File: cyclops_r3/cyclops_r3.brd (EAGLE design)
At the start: 124.5 x 79.9 mm, 107 parts, among them Q1 BC817, Q2 IRF510, U1 MCP4921, U2 MCP4022-50k, U3 317-N, U4 TLV3701, U5 337-N, U6 ADR03, U7 OP1177, U8 LTC2052HV, U9 ZXTD45

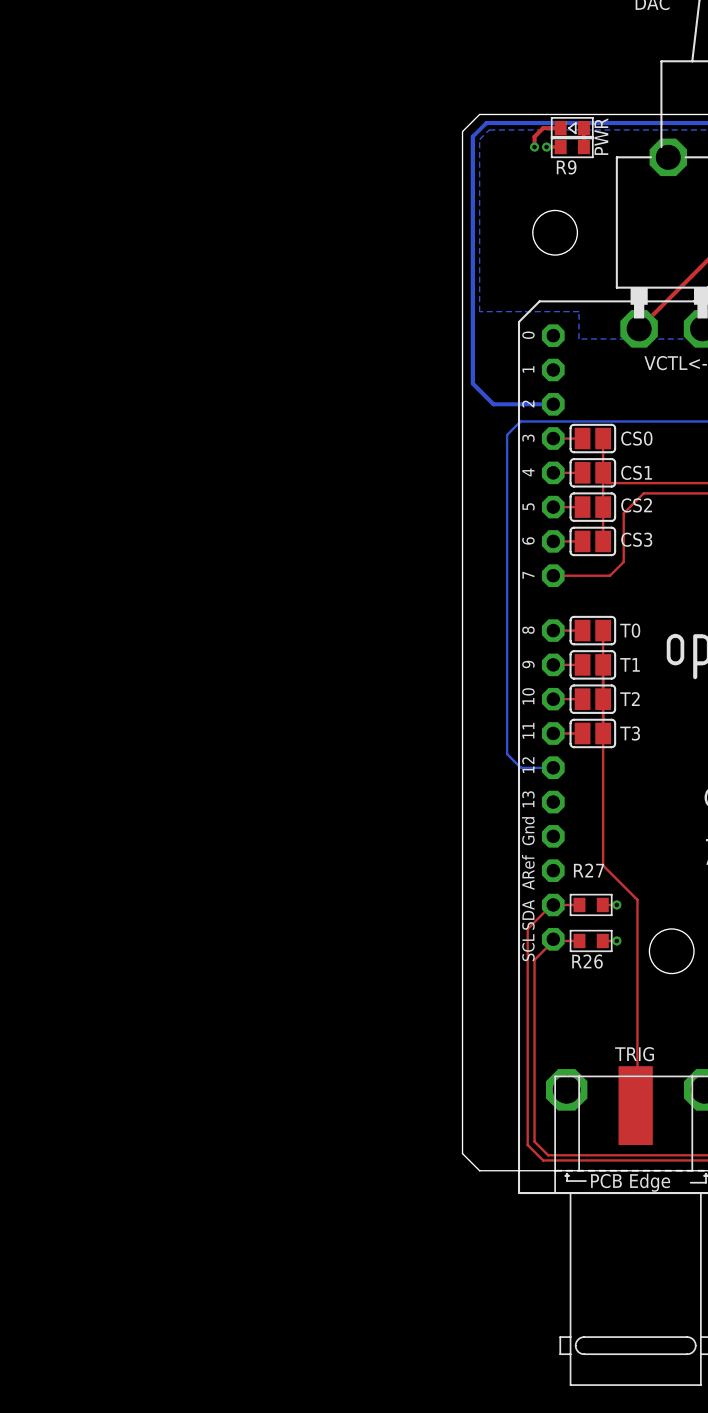
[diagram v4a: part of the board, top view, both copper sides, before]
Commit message: Front panel dimensions have been tested and look good. Started integrating light pipes on front panel LEDs. The LEDs need to be moved and swapped for normal verical ones.
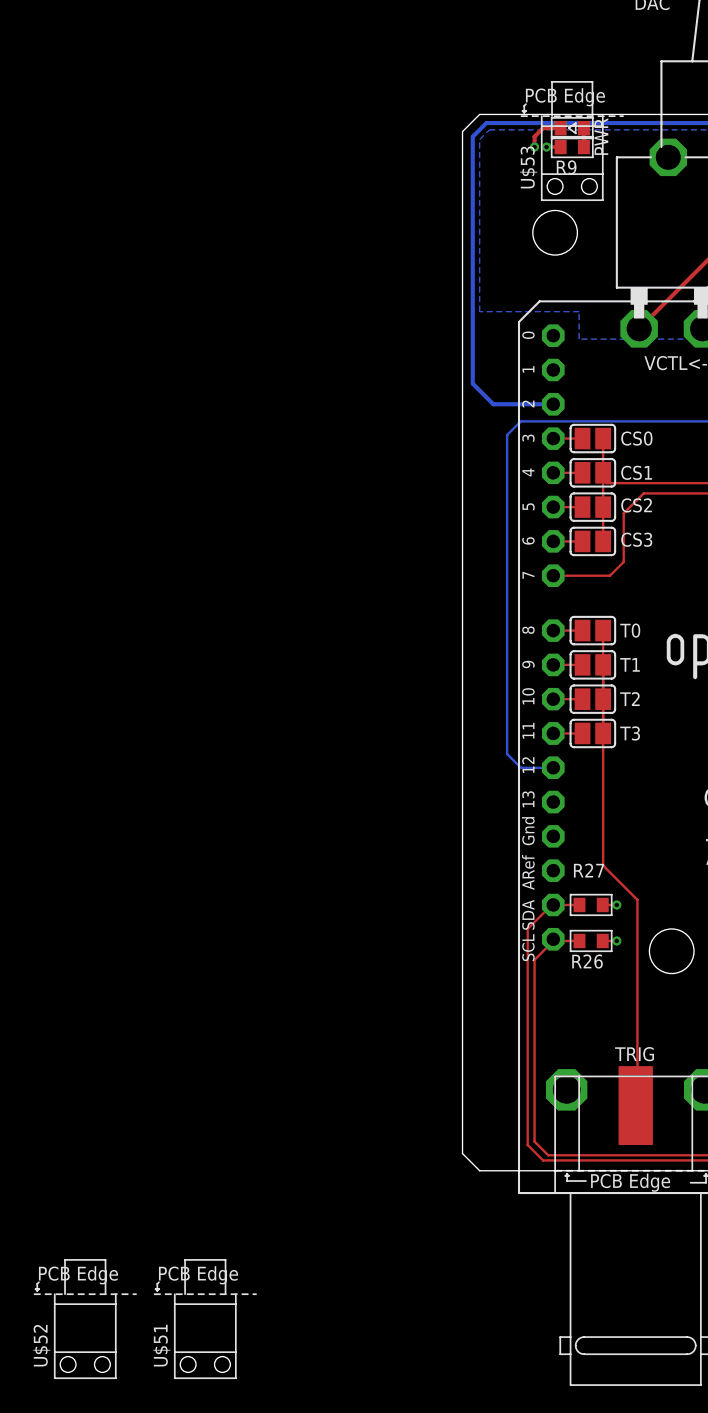
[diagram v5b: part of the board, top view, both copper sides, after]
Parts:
- added U$51, U$52, U$53: SLP3, cyclops:SL3P-150-100-F
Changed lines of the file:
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@@
 <?xml version="1.0" encoding="utf-8"?>
 <!DOCTYPE eagle SYSTEM "eagle.dtd">
-<eagle version="6.6.0">
+<eagle version="6.5.0">
 <drawing>
 <settings>
@@
 <setting verticaltext="up"/>
 </settings>
-<grid distance="0.05" unitdist="inch" unit="inch" style="lines" multiple="1" display="yes" altdistance="0.025" altunitdist="inch" altunit="inch"/>
+<grid distance="0.005" unitdist="inch" unit="inch" style="lines" multiple="1" display="yes" altdistance="0.025" altunitdist="inch" altunit="inch"/>
 <layers>
 <layer number="1" name="Top" color="4" fill="1" visible="yes" active="yes"/>
@@
 <layer number="37" name="tTest" color="7" fill="1" visible="no" active="yes"/>
 <layer number="38" name="bTest" color="7" fill="1" visible="no" active="yes"/>
-<layer number="39" name="tKeepout" color="4" fill="11" visible="no" active="yes"/>
+<layer number="39" name="tKeepout" color="4" fill="11" visible="yes" active="yes"/>
 <layer number="40" name="bKeepout" color="1" fill="11" visible="no" active="yes"/>
 <layer number="41" name="tRestrict" color="4" fill="10" visible="no" active="yes"/>
@@
 <attribute name="VALUE" x="8.128" y="22.733" size="1.016" layer="27" font="vector" ratio="18" align="center-left"/>
 </element>
+<element name="U$51" library="cyclops" package="SL3P-150-100-F" value="SLP3" x="-19.05" y="-12.7"/>
+<element name="U$52" library="cyclops" package="SL3P-150-100-F" value="SLP3" x="-27.94" y="-12.7"/>
+<element name="U$53" library="cyclops" package="SL3P-150-100-F" value="SLP3" x="8.128" y="74.549"/>
 </elements>
 <signals>

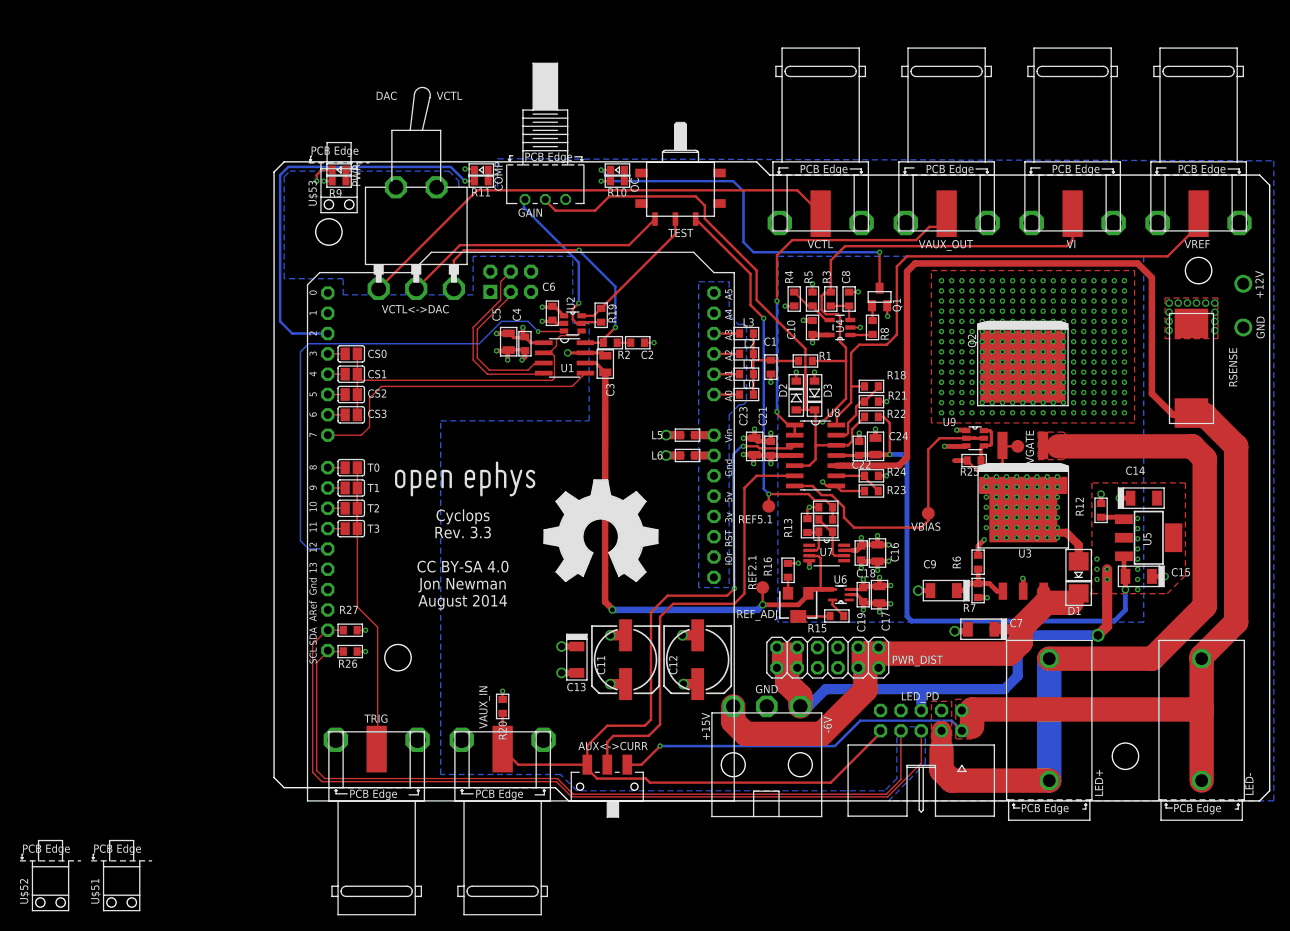
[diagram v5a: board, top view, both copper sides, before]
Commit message: Fixed most of the TODO issues. Need to rearrange front panel layout a bit to acomidate light pipes.
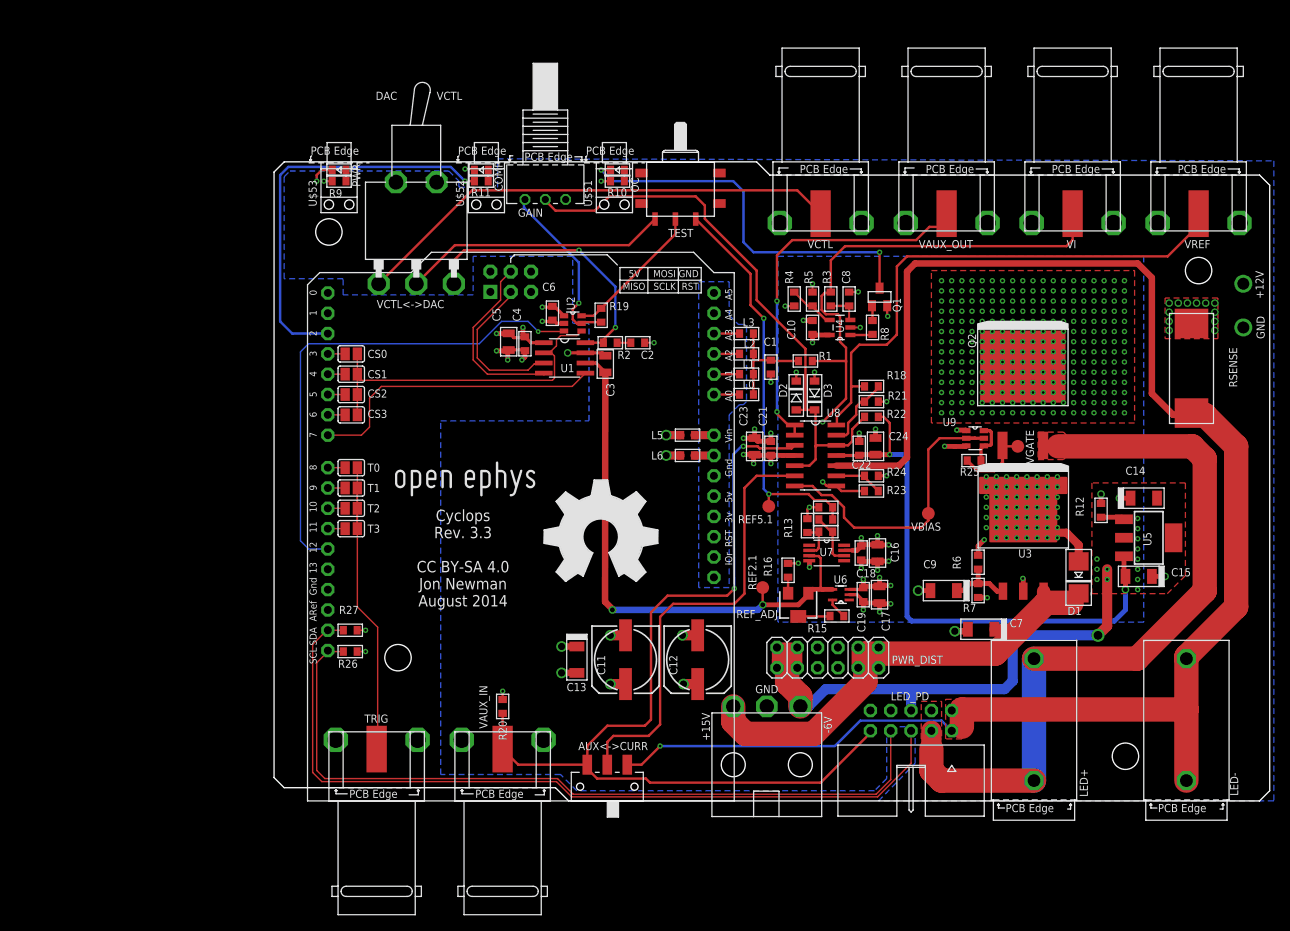
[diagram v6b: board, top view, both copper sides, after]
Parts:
- C1: value .1uF -> 1uF
- R1: value 10k -> 100k
- moved U$51 106.8 mm to (42.5, 74.5)
- moved U$52 102.9 mm to (26.5, 74.5)
- moved LED+ 1.91 mm to (95.0, 2.54)
- moved LED- 1.90 mm to (114.0, 2.54)
- moved LED_PD 1.27 mm to (79.6, 8.76)
- moved VCTL<->DAC 0.63 mm to (17.8, 76.8)
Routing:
- net +15V: track 70.1 -> 68.5 mm
- net N$13: track 11.2 -> 9.58 mm
- net VAUX: track 118.5 -> 117.2 mm
- net SCL: track 98.7 -> 97.5 mm
- net SDA: track 103.7 -> 102.4 mm
- net LED-: track 214.8 -> 213.6 mm
- net DACA: track 36.0 -> 35.4 mm

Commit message: Finished front and rear panel layout. Started PCB version.
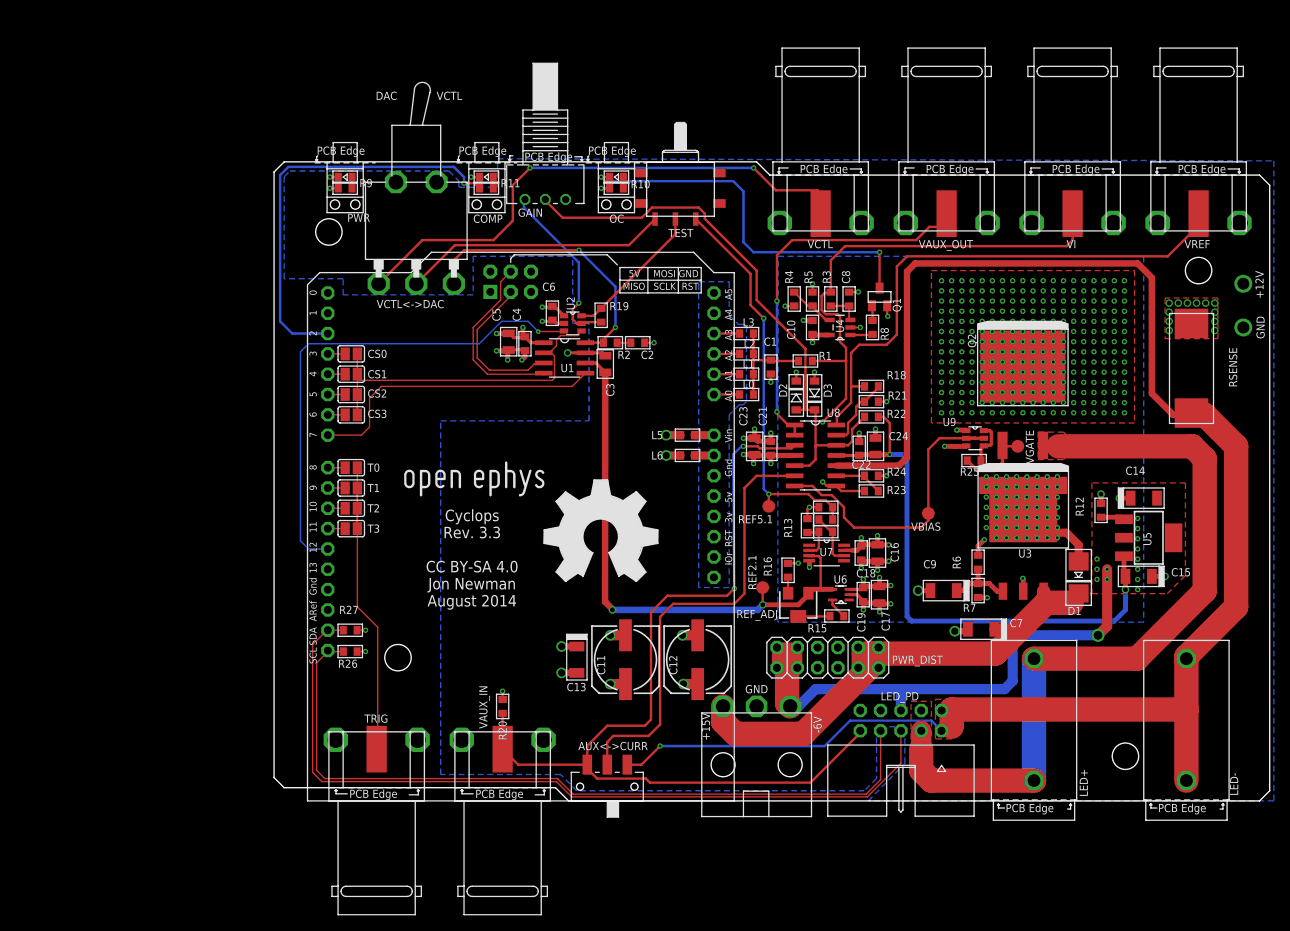
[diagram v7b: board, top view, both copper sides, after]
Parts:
- moved LED_PD 1.27 mm to (78.4, 8.76)
- moved PWR_IN 1.27 mm to (56.1, 4.52)
- moved PWR 1.17 mm to (10.2, 78.0)
- moved R9 1.17 mm to (8.89, 76.6)
- moved U$30 1.14 mm to (15.6, 37.6)
- moved COMP 1.09 mm to (27.8, 78.0)
- moved R11 1.09 mm to (26.5, 76.6)
- moved OC 0.90 mm to (44.1, 78.0)
- moved R10 0.90 mm to (42.8, 76.6)
- moved U$53 0.76 mm to (8.89, 74.5)
- moved U$51 0.25 mm to (42.8, 74.5)
- moved U$52 0.06 mm to (26.6, 74.5)
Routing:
- net VINPUT: track 61.3 -> 67.9 mm, vias 0 -> 2
- net OC_COMP: track 50.3 -> 51.8 mm
- net VAUX: track 117.2 -> 115.9 mm
- net SDA: track 102.4 -> 101.2 mm
- net SCL: track 97.5 -> 96.2 mm
- net LED+: track 93.8 -> 95.1 mm
- net GND: track 113.1 -> 112.0 mm
- net _VREF: track 72.5 -> 71.5 mm
- net +15V: track 68.5 -> 69.4 mm
- net -6V: track 78.9 -> 79.6 mm

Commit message: Minor updates.
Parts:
- VCTL<->DAC: value 2M1 -> 2M1-SP3
- renumbered REF2.1 to REF2.5, REF5.1 to REF5.0
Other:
- board text added: "DISABLE"
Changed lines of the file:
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@@
 <?xml version="1.0" encoding="utf-8"?>
 <!DOCTYPE eagle SYSTEM "eagle.dtd">
-<eagle version="6.5.0">
+<eagle version="6.4">
 <drawing>
 <settings>
@@
 <text x="20.32" y="87.63" size="1.016" layer="21" font="vector" ratio="18">VCTL</text>
 <text x="12.7" y="87.63" size="1.016" layer="21" font="vector" ratio="18">DAC</text>
+<text x="17.78" y="91.44" size="1.016" layer="21" font="vector" ratio="18" rot="R90">DISABLE</text>
 </plain>
 <attributes>
@@
 <attribute name="VALUE" x="87.757" y="77.978" size="1.016" layer="27" font="vector" ratio="18" rot="R180"/>
 </element>
-<element name="REF2.1" library="cyclops" package="TP16R" value="TPTP16R" x="61.08" y="26.67" smashed="yes" rot="R90">
+<element name="REF2.5" library="cyclops" package="TP16R" value="TPTP16R" x="61.08" y="26.67" smashed="yes" rot="R90">
 <attribute name="TP_SIGNAL_NAME" value="" x="62.985" y="26.67" size="1" layer="37" rot="R90"/>
 <attribute name="NAME" x="60.2989" y="26.37" size="1.016" layer="25" font="vector" ratio="18" rot="R90"/>
 </element>
-<element name="REF5.1" library="cyclops" package="TP16R" value="TPTP16R" x="61.842" y="36.83" smashed="yes" rot="R90">
+<element name="REF5.0" library="cyclops" package="TP16R" value="TPTP16R" x="61.842" y="36.83" smashed="yes" rot="R90">
 <attribute name="TP_SIGNAL_NAME" value="" x="63.747" y="36.83" size="1" layer="37" rot="R90"/>
 <attribute name="NAME" x="57.993" y="34.6971" size="1.016" layer="25" font="vector" ratio="18"/>
@@
 <attribute name="VALUE" x="35.306" y="73.025" size="1.016" layer="27" font="vector" ratio="18"/>
 </element>
-<element name="VCTL&lt;-&gt;DAC" library="cyclops" package="2M1-SP1-T2-B4-M6RE" value="2M1" x="17.78" y="76.835" smashed="yes" rot="R270">
+<element name="VCTL&lt;-&gt;DAC" library="cyclops" package="2M1-SP1-T2-B4-M6RE" value="2M1-SP3" x="17.78" y="76.835" smashed="yes" rot="R270">
 <attribute name="NAME" x="12.827" y="61.595" size="1.016" layer="25" font="vector" ratio="18"/>
-<attribute name="VALUE" x="16.383" y="74.549" size="1.016" layer="27" font="vector" ratio="18"/>
+<attribute name="VALUE" x="15.113" y="74.549" size="1.016" layer="27" font="vector" ratio="18"/>
 </element>
 <element name="L6" library="cyclops" package="0603" value="MPZ1608" x="51.689" y="43.18" smashed="yes" rot="R180">
@@
 <contactref element="U6" pad="4"/>
 <contactref element="REF_ADJ" pad="1"/>
-<contactref element="REF2.1" pad="TP"/>
+<contactref element="REF2.5" pad="TP"/>
 <wire x1="69.8176" y1="26.4414" x2="68.58" y2="26.4414" width="0.6096" layer="1"/>
 <wire x1="68.58" y1="26.4414" x2="67.2754" y2="26.4414" width="0.6096" layer="1"/>
@@
 <contactref element="R17" pad="2"/>
 <contactref element="C20" pad="1"/>
-<contactref element="REF5.1" pad="TP"/>
+<contactref element="REF5.0" pad="TP"/>
 <wire x1="59.563" y1="61.976" x2="61.214" y2="60.325" width="0.3048" layer="1"/>
 <wire x1="69.8246" y1="35.179" x2="69.8246" y2="36.703" width="0.3048" layer="1"/>
@@
 </signal>
 </signals>
-<errors>
-</errors>
 </board>
 </drawing>
